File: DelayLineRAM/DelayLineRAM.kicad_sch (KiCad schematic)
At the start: 38 parts, among them J1 IO Connector Pins, Q1 NPN, U1 SR 1, U10 SR 10, U11 SR 11, U12 SR 12, U13 SR 13, U14 SR 14, U15 SR 15, U16 SR 16, U17 SR 17, U18 SR 18, U19 SR 19, U2 SR 2, U20 SR 20, U21 SR 21, U22 SR 22, U23 SR 23, U24 SR 24, U25 SR 25, U26 SR 26, U27 SR 27, U28 SR 28, U29 SR 29, U3 SR 3, U30 SR 30, U31 SR 31, U32 SR 32, U4 SR 4, U5 SR 5, U6 SR 6, U7 SR 7, U8 SR 8, U9 SR 9

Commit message: Finished the Address Counter PCB
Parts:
- added TP1, TP2, TP3, TP4, TP5, TP6, TP7: TestPoint, TestPoint:TestPoint_Pad_D1.5mm, symbol Connector:TestPoint
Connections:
- net +5V: now also TP1.1
- net Clock: now also TP5.1
- net DataIn: now also TP3.1
- net DataOut: now also TP4.1
- net DoWrite: now also TP7.1
- net GND: now also TP2.1
- net Reset renamed Reset#
- net Reset#: now also TP6.1
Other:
- moved on the sheet: U16, U24, U25, U32

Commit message: changed ram connector to pin headers and created fab data for the delay line ram
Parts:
- J1: footprint Connector_Hirose:Hirose_DF13-07P-1.25DSA_1x07_P1.25mm_Vertical -> Connector_PinHeader_2.54mm:PinHeader_1x07_P2.54mm_Horizontal
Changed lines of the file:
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@@
 			)
 		)
-		(property "Footprint" "Connector_Hirose:Hirose_DF13-07P-1.25DSA_1x07_P1.25mm_Vertical"
+		(property "Footprint" "Connector_PinHeader_2.54mm:PinHeader_1x07_P2.54mm_Horizontal"
 			(at 40.64 90.17 0)
 			(effects

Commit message: remove old fab files for DLR so i can update the mux line selection circuit
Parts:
- added Q2, Q3: NPN, Package_TO_SOT_THT:TO-92, symbol Simulation_SPICE:NPN
- added R3, R4, R5, R6: 1kOhm, Resistor_THT:R_Axial_DIN0204_L3.6mm_D1.6mm_P5.08mm_Horizontal, symbol Device:R
- R1: value 10kOhm -> 1kOhm
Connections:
- net +5V: now also R5.2
- net DataIn: now also R4.2; no longer D1.2 (A)
- net GND: now also Q2.3 (E), Q3.3 (E)
- net DoWrite renamed WriteEnable
- net WriteEnable: now also R6.1
- new net: D1.2 (A), Q2.1 (C), R4.1
- new net: Q2.2 (B), R3.1
- new net: Q3.2 (B), R6.2
- new net !WriteEnable: Q3.1 (C), R3.2, R5.1
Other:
- note added: "<--- If WriteEnable is Low (0v) then it'll pull this low"
- note added: "If WriteEnable is High (5v) then it'll pull this low --->"
- note added: "Invert the WriteEnable signal for the selection of LastSR_Out or DataIn"
- note removed: "<--- If DoWrite is High (5v) then it'll pull the wire after SR16_Out low meaning DataIn will take "priority""
- moved on the sheet: D1, D2, Q1, R2

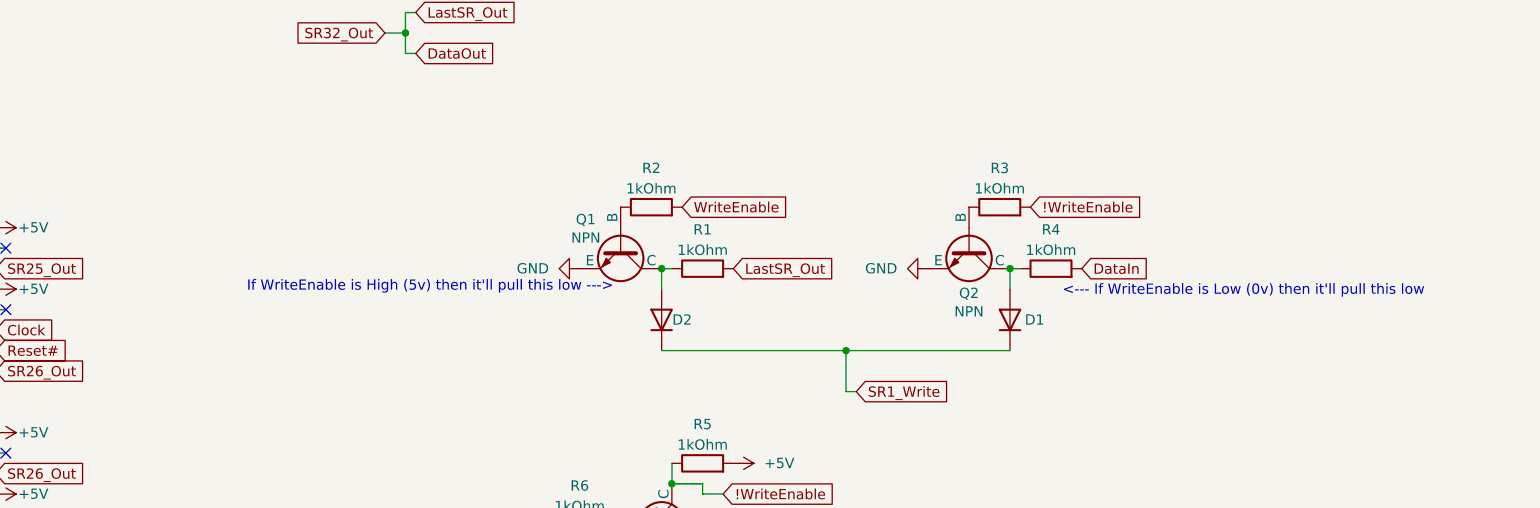
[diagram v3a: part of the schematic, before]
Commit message: fixed the circuit in kicad for the schem and pcb
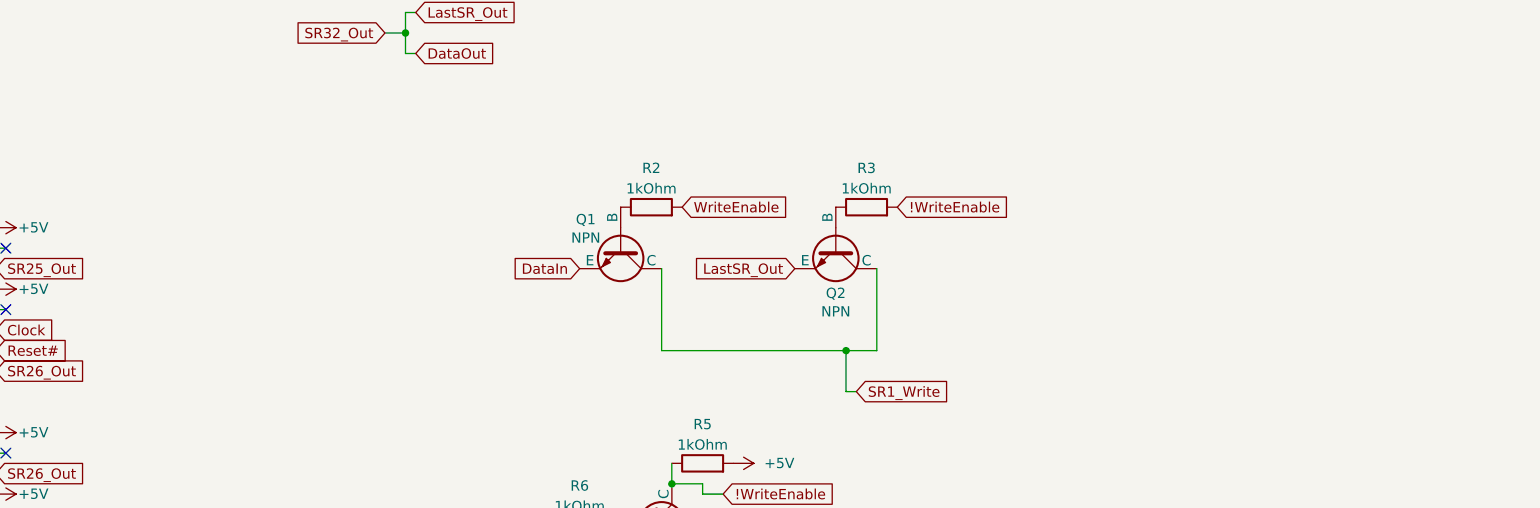
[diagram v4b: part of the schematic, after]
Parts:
- removed D1, D2: D, Diode_THT:D_5W_P12.70mm_Horizontal, symbol Device:D
- removed R1, R4: 1kOhm, Resistor_THT:R_Axial_DIN0204_L3.6mm_D1.6mm_P5.08mm_Horizontal, symbol Device:R
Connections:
- net DataIn: now also Q1.3 (E)
- net DataOut: now also Q2.3 (E)
- net GND: no longer Q1.3 (E), Q2.3 (E)
- net SR1_Write: now also Q1.1 (C), Q2.1 (C)
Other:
- note removed: "<--- If WriteEnable is Low (0v) then it'll pull this low"
- note removed: "If WriteEnable is High (5v) then it'll pull this low --->"
- moved on the sheet: Q2, R3
